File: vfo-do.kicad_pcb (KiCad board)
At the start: 2 copper layers, 100 x 50 mm, 29 parts, among them P1 CONN_01X02, P2 Band, P3 Si5351, P4 Encoder, P5 GPS, P6 CONN_01X09, U1 LM317T, U2 MC78M05CDT, U3 MC78M05CDT, U4 Arduino_Nano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

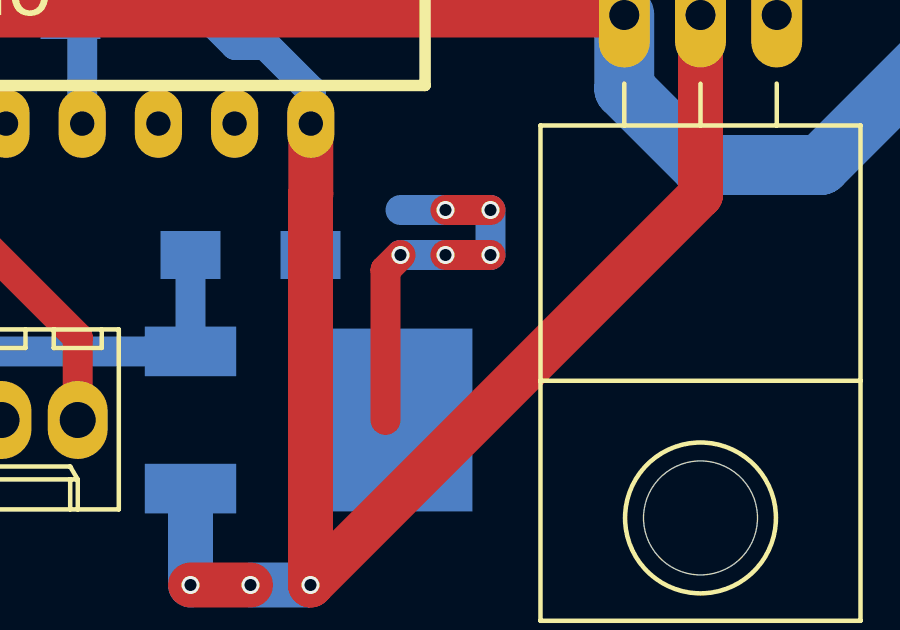
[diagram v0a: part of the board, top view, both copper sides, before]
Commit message: modif du rappel de masse d'un rétulateur 5V
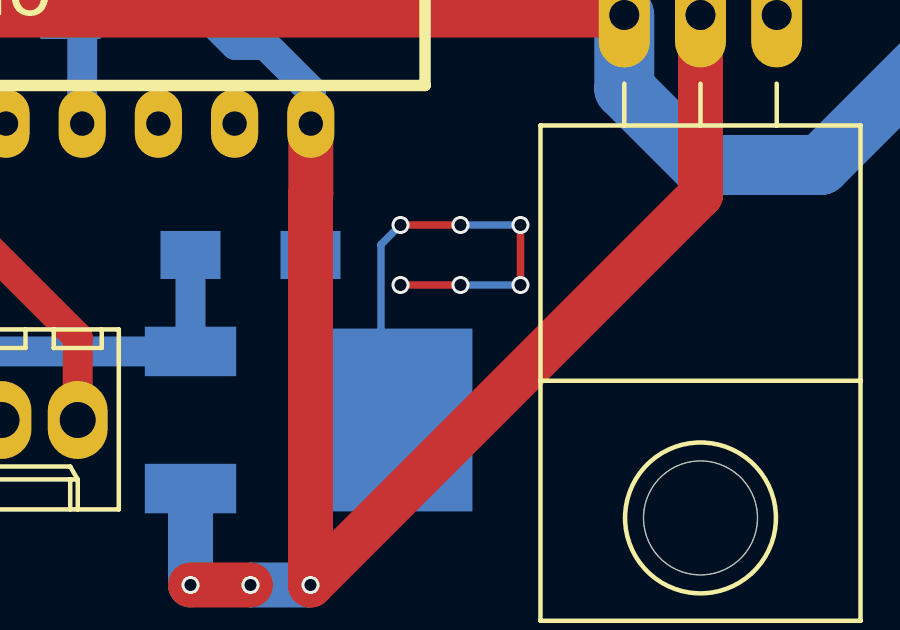
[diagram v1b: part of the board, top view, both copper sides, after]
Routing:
- net GND: track 55.3 -> 72.1 mm, vias 24 -> 30
- net (no net): track 13.2 -> 0.00 mm, vias 5 -> 0
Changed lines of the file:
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@@
     (links 89)
     (no_connects 1)
-    (area 85.924999 73.924999 191.075001 197.575001)
+    (area 90.924999 73.924999 191.075001 124.075001)
     (thickness 1.6)
     (drawings 10)
-    (tracks 361)
+    (tracks 362)
     (zones 0)
     (modules 29)
@@
     (arrow2b (pts (xy 191 67) (xy 189.873496 67.586421)))
   )
-  (segment (start 165.5 113.5) (end 165.5 108.5) (width 1) (layer F.Cu) (net 0))
-  (segment (start 167.5 106.5) (end 166 106.5) (width 1) (layer B.Cu) (net 0))
-  (via (at 167.5 106.5) (size 0.6) (drill 0.4) (layers F.Cu B.Cu) (net 0))
-  (segment (start 169 106.5) (end 167.5 106.5) (width 1) (layer F.Cu) (net 0))
-  (via (at 169 106.5) (size 0.6) (drill 0.4) (layers F.Cu B.Cu) (net 0))
-  (segment (start 169 108) (end 169 106.5) (width 1) (layer B.Cu) (net 0))
-  (via (at 169 108) (size 0.6) (drill 0.4) (layers F.Cu B.Cu) (net 0))
-  (segment (start 167.5 108) (end 169 108) (width 1) (layer F.Cu) (net 0))
-  (via (at 167.5 108) (size 0.6) (drill 0.4) (layers F.Cu B.Cu) (net 0))
-  (segment (start 166 108) (end 167.5 108) (width 1) (layer B.Cu) (net 0))
-  (via (at 166 108) (size 0.6) (drill 0.4) (layers F.Cu B.Cu) (net 0))
-  (segment (start 165.5 108.5) (end 166 108) (width 1) (layer F.Cu) (net 0))
   (segment (start 186 100.29998) (end 184.70002 100.29998) (width 2) (layer B.Cu) (net 1))
   (segment (start 173.46 102.46) (end 173.46 100) (width 2) (layer B.Cu) (net 1))
@@
   (segment (start 111.78 102) (end 111.58 102.2) (width 0.5) (layer B.Cu) (net 1))
   (segment (start 129 113.5) (end 129 117) (width 1) (layer B.Cu) (net 1))
+  (segment (start 165.35 113.5) (end 165.35 107.65) (width 0.25) (layer B.Cu) (net 2) (status 400000))
+  (via (at 166 109) (size 0.6) (drill 0.4) (layers F.Cu B.Cu) (net 2))
+  (segment (start 168 109) (end 166 109) (width 0.25) (layer F.Cu) (net 2))
+  (via (at 168 109) (size 0.6) (drill 0.4) (layers F.Cu B.Cu) (net 2))
+  (segment (start 170 109) (end 168 109) (width 0.25) (layer B.Cu) (net 2))
+  (via (at 170 109) (size 0.6) (drill 0.4) (layers F.Cu B.Cu) (net 2))
+  (segment (start 170 107) (end 170 109) (width 0.25) (layer F.Cu) (net 2))
+  (via (at 170 107) (size 0.6) (drill 0.4) (layers F.Cu B.Cu) (net 2))
+  (segment (start 168 107) (end 170 107) (width 0.25) (layer B.Cu) (net 2))
+  (via (at 168 107) (size 0.6) (drill 0.4) (layers F.Cu B.Cu) (net 2))
+  (segment (start 166 107) (end 168 107) (width 0.25) (layer F.Cu) (net 2))
+  (via (at 166 107) (size 0.6) (drill 0.4) (layers F.Cu B.Cu) (net 2))
+  (segment (start 165.35 107.65) (end 166 107) (width 0.25) (layer B.Cu) (net 2))
   (segment (start 111.58 92.8) (end 111.58 93.08) (width 0.5) (layer B.Cu) (net 2))
   (segment (start 111.58 93.08) (end 112.5 94) (width 0.5) (layer B.Cu) (net 2))

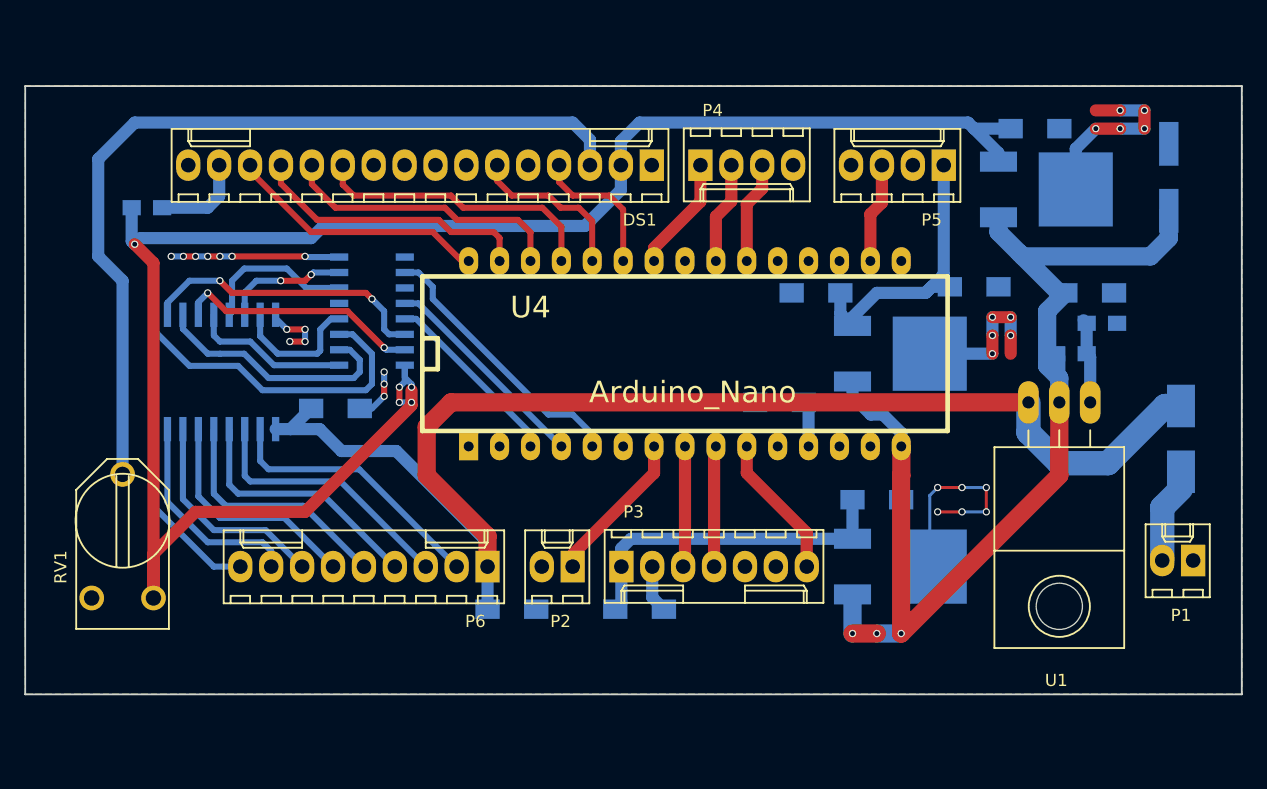
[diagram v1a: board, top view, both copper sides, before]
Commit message: suppression des sorties filtres
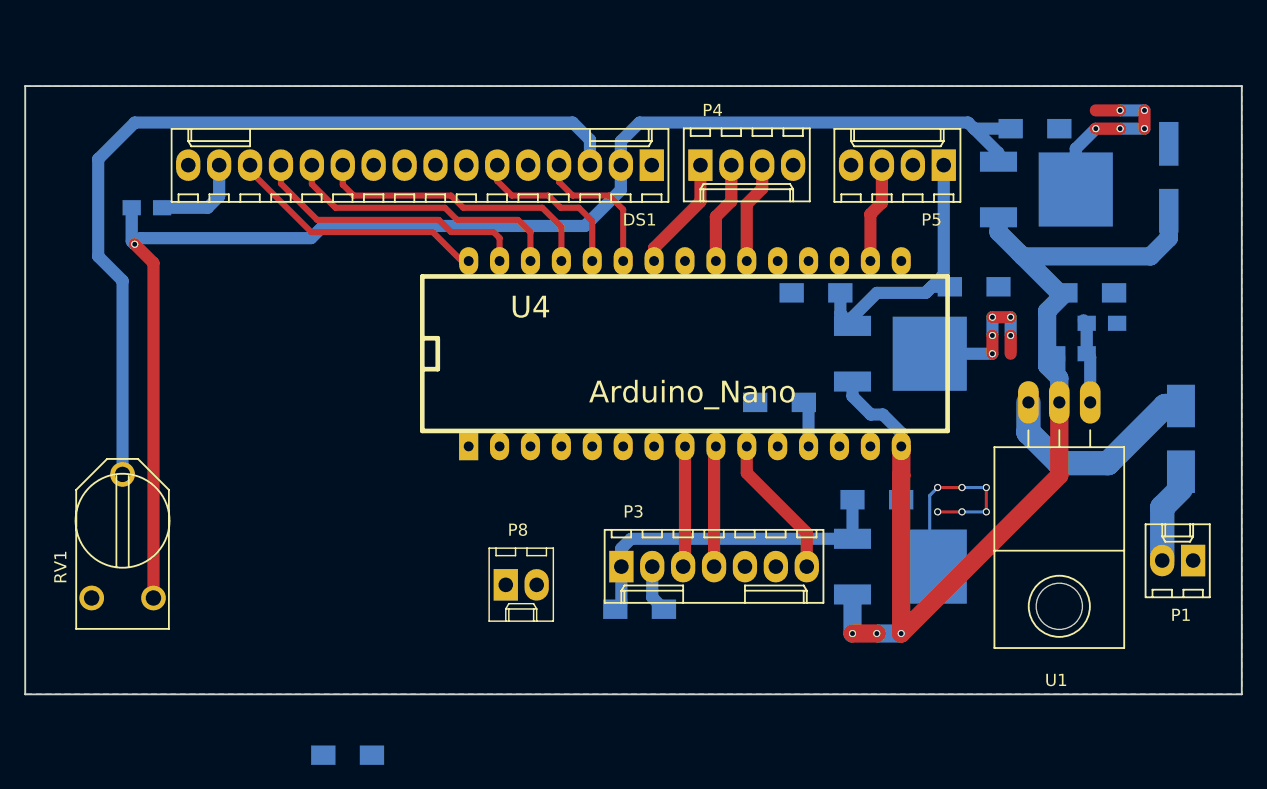
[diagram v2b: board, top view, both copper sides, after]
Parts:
- removed C8: 100n, Capacitors_SMD:C_1206_HandSoldering
- removed P2: Band, Connectors_Molex:Molex_KK_6410-02
- removed P6: CONN_01X09, Connectors_Molex:Molex_KK_6410-09
- removed U5: ULN2803A, Housings_SOIC:SOIC-18_7.5x11.6mm_Pitch1.27mm
- removed U6: 4028, Housings_SOIC:SOIC-16_3.9x9.9mm_Pitch1.27mm
- added P8: Reset, Connectors_Molex:Molex_KK-6410-02_02x2.54mm_Straight, F.Cu at (130.5, 115.0)
- moved C1 18.1 mm to (117.5, 129.0)
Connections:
- net Net-(C2-Pad1) renamed +8V
- net Net-(C6-Pad1) renamed +5C
- net Net-(D1-Pad2) renamed +12V
- net VDD renamed +5P
- U4 pad 10: Net-(P3-Pad7) -> (no net)
- U4 pad 18: (no net) -> Net-(P8-Pad1)
- U4 pad 23: (no net) -> Net-(P3-Pad7)
- U4 pad 3: Net-(U4-Pad3) -> (no net)
- U4 pad 4: Net-(U4-Pad4) -> (no net)
- U4 pad 5: Net-(U4-Pad5) -> (no net)
- U4 pad 7: Net-(P2-Pad1) -> (no net)
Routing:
- net Net-(C1-Pad1): track 111.3 -> 18.0 mm
- net +5P: track 154.8 -> 116.1 mm, vias 5 -> 1
- net Net-(U5-Pad1): track 27.4 -> 0.00 mm
- net Net-(U5-Pad2): track 24.0 -> 0.00 mm, vias 2 -> 0
- net GND: track 72.1 -> 48.5 mm, vias 30 -> 16
- net Net-(U4-Pad5): track 22.5 -> 0.00 mm
- net Net-(P6-Pad2): track 22.4 -> 0.00 mm
- net Net-(P6-Pad3): track 21.8 -> 0.00 mm
- net Net-(P6-Pad4): track 21.0 -> 0.00 mm
- net Net-(U5-Pad3): track 20.6 -> 0.00 mm
- net Net-(U5-Pad4): track 20.3 -> 0.00 mm, vias 2 -> 0
- net Net-(P6-Pad5): track 20.1 -> 0.00 mm
- net Net-(P6-Pad6): track 19.0 -> 0.00 mm
- net Net-(P6-Pad7): track 17.9 -> 0.00 mm
- net Net-(U4-Pad4): track 17.7 -> 0.00 mm
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
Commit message: nettoyage routage, LM317 et Si5351 non verifie
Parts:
- added P2: DWN, Connectors_Molex:Molex_KK-6410-02_02x2.54mm_Straight, F.Cu at (117.5, 109.5)
- added P6: UP, Connectors_Molex:Molex_KK-6410-02_02x2.54mm_Straight, F.Cu at (124.0, 109.5)
- added P7: Band, Connectors_Molex:Molex_KK-6410-02_02x2.54mm_Straight, F.Cu at (130.5, 109.5)
- C4, R3: moved to F.Cu
- DS1: footprint Connectors_Molex:Molex_KK_6410-16 -> Connectors_Molex:Molex_KK-6410-16_16x2.54mm_Straight
- P1: value CONN_01X02 -> 12V in; footprint Connectors_Molex:Molex_KK_6410-02 -> Connectors_Molex:Molex_KK-6410-02_02x2.54mm_Straight
- P3: footprint Connectors_Molex:Molex_KK_6410-07 -> Connectors_Molex:Molex_KK-6410-07_07x2.54mm_Straight
- P4, P5: footprint Connectors_Molex:Molex_KK_6410-04 -> Connectors_Molex:Molex_KK-6410-04_04x2.54mm_Straight
- moved C1 70.0 mm to (179.0, 95.5), turned to 90 degrees
- moved RV1 18.0 mm to (112.0, 98.5), turned to 270 degrees
- moved P8 17.9 mm to (113.5, 109.5), turned to 180 degrees
- moved R3 9.01 mm to (109.5, 87.0), turned to 270 degrees
- moved C3 8.06 mm to (134.5, 113.0), turned to 0 degrees
- moved U3 6.73 mm to (164.0, 109.0), turned to 270 degrees
- moved P1 6.52 mm to (181.5, 109.5), turned to 0 degrees
- moved C10 5.00 mm to (171.0, 73.5)
- moved C2 5.00 mm to (175.5, 87.0)
- moved C5 5.00 mm to (150.0, 96.0)
- moved C6 5.00 mm to (166.0, 86.5)
- moved C7 5.00 mm to (153.0, 87.0)
- moved C9 5.00 mm to (158.0, 112.0), turned to 90 degrees
- moved D1 5.00 mm to (183.0, 99.0)
- moved DS1 5.00 mm to (139.5, 76.5)
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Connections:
- RV1 pad 1: GND -> +5P
- RV1 pad 3: +5P -> GND
- U4 pad 13: (no net) -> Net-(P8-Pad1)
- U4 pad 18: Net-(P8-Pad1) -> (no net)
- U4 pad 4: (no net) -> Net-(P2-Pad1)
- U4 pad 5: (no net) -> Net-(P6-Pad1)
- U4 pad 7: (no net) -> Net-(P7-Pad1)
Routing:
- net GND: track 48.5 -> 355.3 mm, vias 16 -> 53
- net Net-(P8-Pad1): track 0.00 -> 47.5 mm
- net Net-(P3-Pad7): track 11.9 -> 51.8 mm
- net +5P: track 116.1 -> 81.2 mm, vias 1 -> 0
- net Net-(DS1-Pad3): track 72.2 -> 45.2 mm
- net Net-(P2-Pad1): track 0.00 -> 22.4 mm
- net Net-(P6-Pad1): track 0.00 -> 18.1 mm
- net +8V: track 92.0 -> 74.1 mm, vias 3 -> 1
- net Net-(P7-Pad1): track 0.00 -> 17.2 mm
- net Net-(P5-Pad2): track 0.00 -> 16.9 mm
- net (no net): track 2.10 -> 16.7 mm, vias 0 -> 6
- net Net-(C3-Pad2): track 27.7 -> 41.9 mm
- net Net-(C1-Pad1): track 18.0 -> 24.8 mm
- net Net-(DS1-Pad15): track 7.64 -> 11.6 mm
- net +12V: track 6.54 -> 8.23 mm
